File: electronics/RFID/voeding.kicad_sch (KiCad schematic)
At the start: 10 parts, among them J3 USB_C_Receptacle_PowerOnly_6P, U1 AP63200WU

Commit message: hallo allemaal, dit is de meest recente versie van het KiCad project. Hopelijk snappen jullie mijn aanpassingen zodat we de samenwerking goed kunnen verderzetten. Groetjes van jullie teamgenoot, Robbe De Voet
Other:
- moved on the sheet: R6

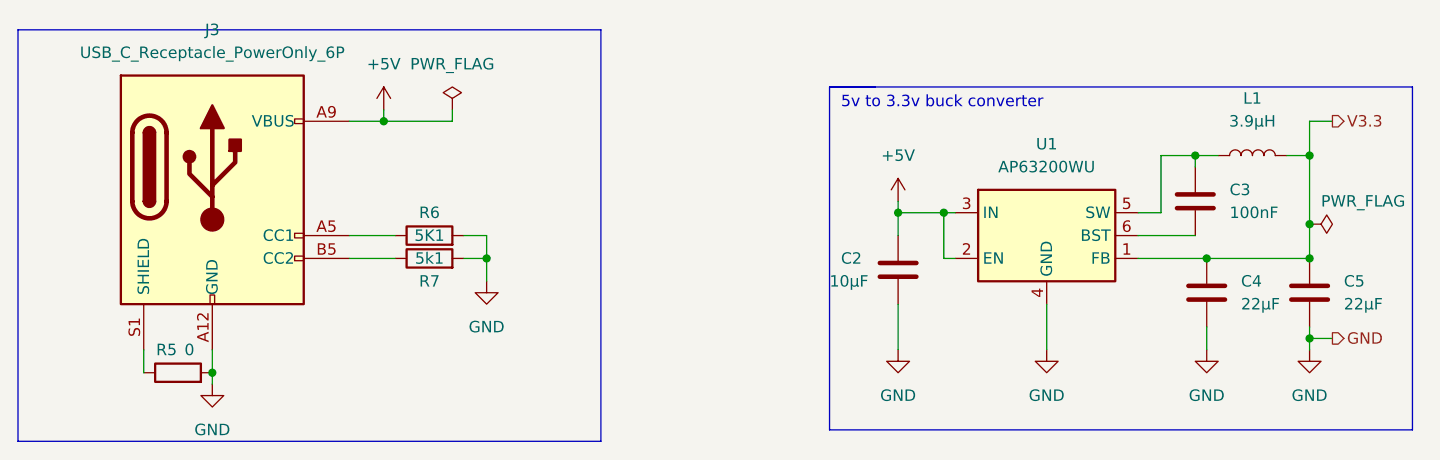
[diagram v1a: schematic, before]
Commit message: added tcp connection and device tab
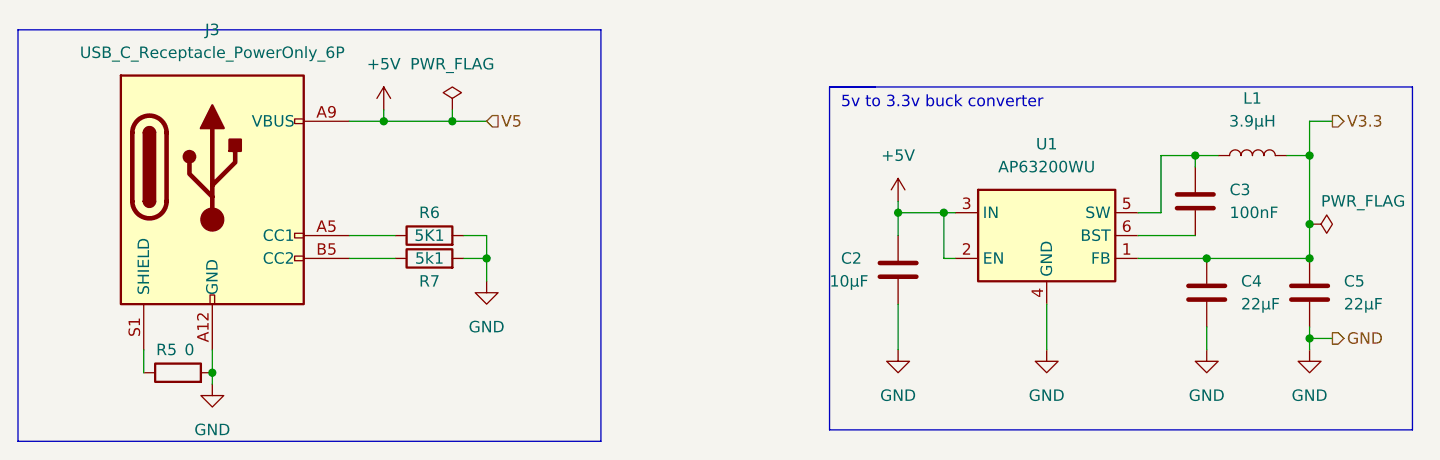
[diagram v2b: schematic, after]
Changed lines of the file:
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@@
   (junction (at 209.55 73.66) (diameter 0) (color 0 0 0 0)
+  )
+  (junction (at 125.73 58.42) (diameter 0) (color 0 0 0 0)
   )
   (wire (pts (xy 99.06 86.36) (xy 99.06 87.63))
@@
   )
   (wire (pts (xy 181.61 73.66) (xy 180.34 73.66))
+    (stroke (width 0) (type default))
+  )
+  (wire (pts (xy 125.73 58.42) (xy 129.54 58.42))
     (stroke (width 0) (type default))
   )
@@
     (effects (font (size 1.27 1.27)) (justify left bottom))
   )
+  (hierarchical_label "V5" (shape input) (at 129.54 58.42 0) (fields_autoplaced)
+    (effects (font (size 1.27 1.27)) (justify left))
+  )
   (hierarchical_label "V3.3" (shape output) (at 223.52 58.42 0) (fields_autoplaced)
